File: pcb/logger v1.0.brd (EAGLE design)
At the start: 59.8 x 53.3 mm, 29 parts, among them J1 MICRO-SDCARD-CONNECTOR-330006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, K1 RESET, U1 DS1307ZN-1900100P1, U2 CJ1117-3.3-1310190P1, U3 74VHCT125PW, X1 32.768KHZ

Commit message: Mostly wired up
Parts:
- turned I2C to 90 degrees
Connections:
- new net AREF: JP2.1, U$4.AREF
- new net D2: JP4.3, U$4.D2
- new net D3: JP4.4, U$4.D3
- new net D4: JP4.5, U$4.D4
- new net D5: JP4.6, U$4.D5
- new net D6: JP4.7, U$4.D6
- new net D7: JP4.8, U$4.D7
- new net D8: JP2.8, U$4.D8
- new net D9: JP2.7, U$4.D9
- new net N$55: U$4.SCL
- new net N$87: U$4.SDA
- new net RX: JP4.1, U$4.RX
- new net TX: JP4.2, U$4.TX
- net +3V3: now also U$4.3.3V
- net +5V: now also U$4.5V
- net GND: now also U$4.GND@0, U$4.GND@1, U$4.GND@2
- net MISO: now also U$4.D12
- net MOSI: now also U$4.D11
- net RESET: now also U$4.RES
- net SCK: now also U$4.D13
- net SD_CS: now also U$4.D10
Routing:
- net SD_CS: track 113.8 -> 71.0 mm, vias 1 -> 4
- net +5V: track 107.6 -> 140.0 mm, vias 3 -> 0
- net SCK: track 78.5 -> 102.3 mm, vias 0 -> 1
- net +3V3: track 90.4 -> 70.7 mm, vias 2 -> 0
- net GND: track 27.7 -> 44.8 mm, vias 0 -> 4
- net MISO: track 64.9 -> 76.4 mm, vias 0 -> 1
- net N$20: track 39.4 -> 49.2 mm, vias 0 -> 1
- net MOSI: track 77.4 -> 71.9 mm
- net SD_DATAIN: track 10.9 -> 15.9 mm, vias 0 -> 2
- net AREF: track 0.00 -> 3.77 mm
- net TX: track 0.00 -> 3.77 mm
- net D9: track 0.00 -> 3.77 mm
- net D8: track 0.00 -> 3.77 mm
- net D7: track 0.00 -> 3.77 mm
- net D5: track 0.00 -> 3.77 mm
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- added copper zone on layer 16, net GND

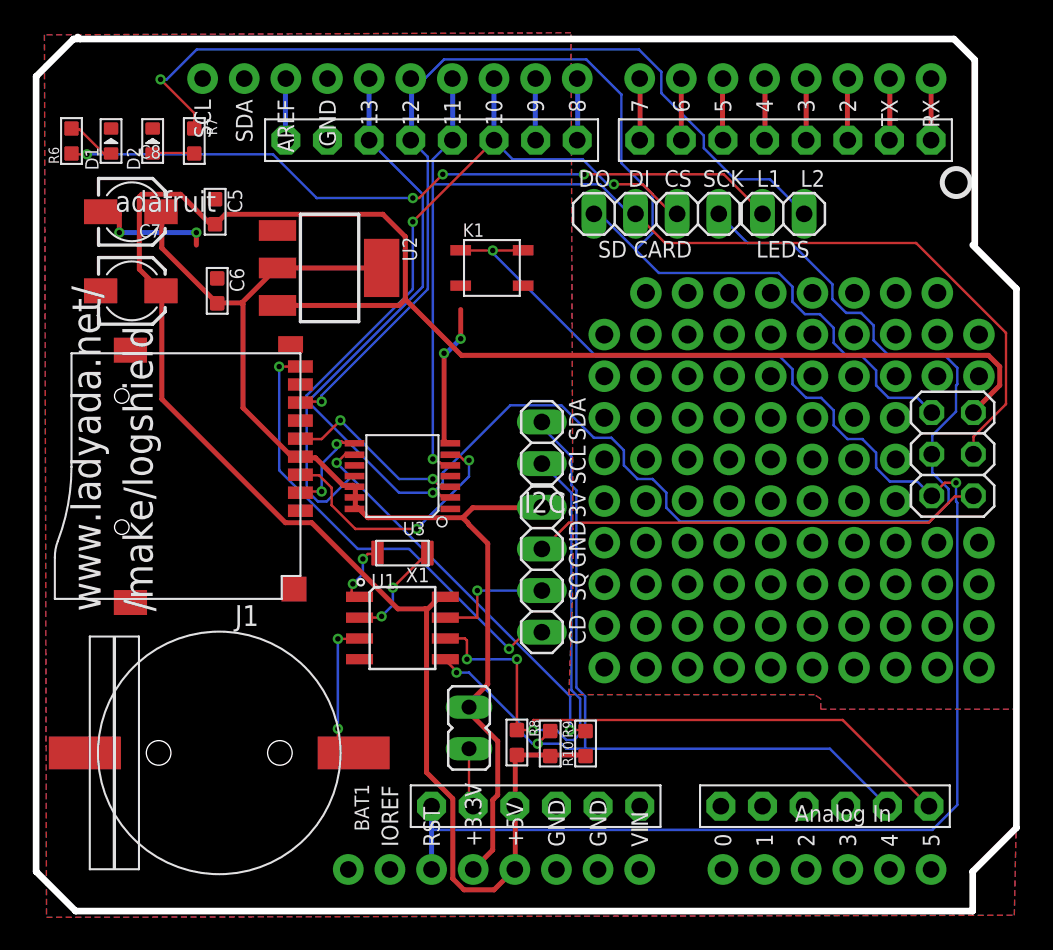
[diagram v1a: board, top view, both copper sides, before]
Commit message: Added extra LED's, finished wiring
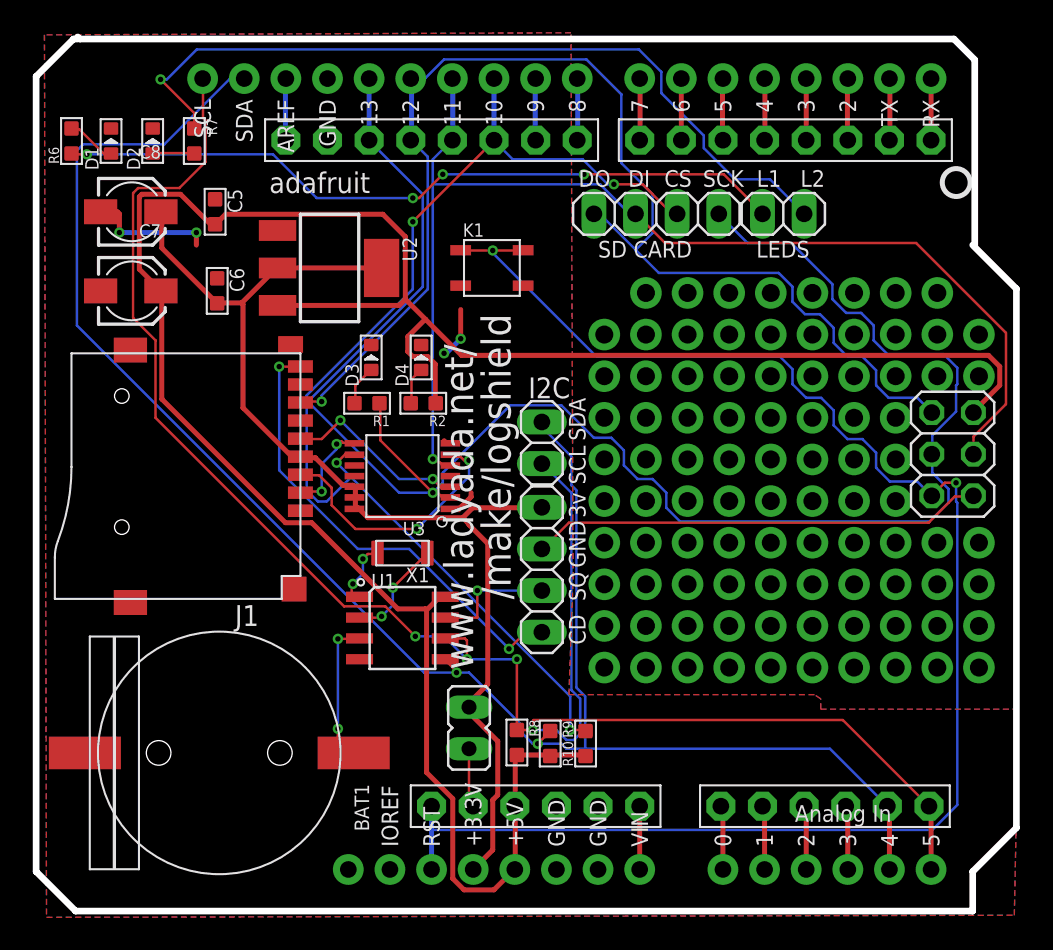
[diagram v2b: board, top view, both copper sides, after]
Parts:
- added D3: CLK, Discrete:LED-0603
- added D4: POWER, Discrete:LED-0603
- added R1, R2: 1k, Discrete:R0603
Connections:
- removed net N$55: U$4.SCL
- removed net N$87: U$4.SDA
- new net A0: JP9.1, U$4.A0
- new net A1: JP9.2, U$4.A1
- new net A2: JP9.3, U$4.A2
- new net A3: JP9.4, U$4.A3
- new net N$26: D3.+, R1.2
- new net N$40: D4.+, R2.2
- new net VIN: JP7.1, U$4.VIN
- net +5V: now also R2.1
- net GND: now also D3.-, D4.-
- net RTC_SCL: now also U$4.A5, U$4.SCL
- net RTC_SDA: now also U$4.A4, U$4.SDA
- net SCK: now also R1.1
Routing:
- net RTC_SDA: track 53.2 -> 111.8 mm
- net RTC_SCL: track 58.6 -> 112.3 mm, vias 3 -> 4
- net +5V: track 140.0 -> 146.8 mm
- net SCK: track 102.3 -> 109.1 mm
- net A1: track 0.00 -> 3.99 mm
- net A0: track 0.00 -> 3.99 mm
- net A3: track 0.00 -> 3.99 mm
- net A2: track 0.00 -> 3.99 mm
- net VIN: track 0.00 -> 3.86 mm
- net GND: track 44.8 -> 41.3 mm
- net N$26: track 0.00 -> 2.47 mm
- net N$40: track 0.00 -> 2.32 mm

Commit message: Changed and rerouted to match OPL availability
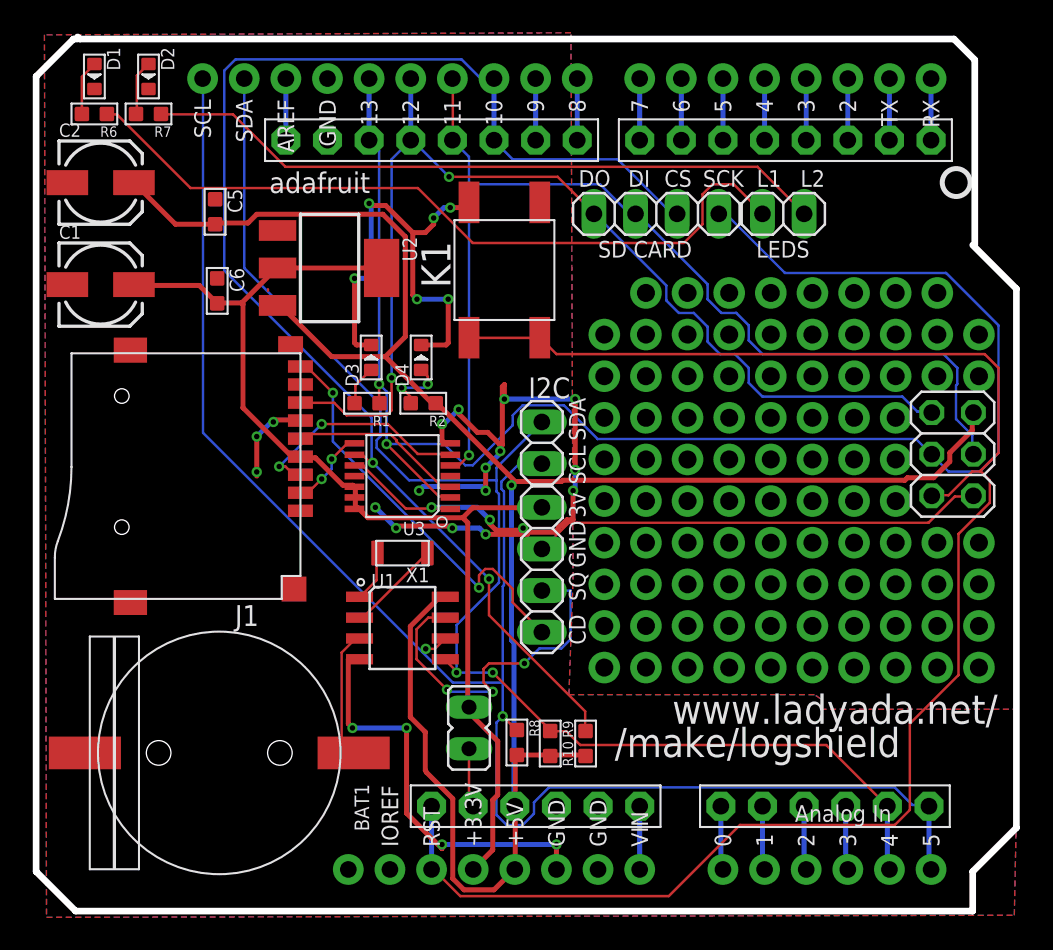
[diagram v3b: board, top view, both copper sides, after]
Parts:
- removed C7, C8: 100uF, Discrete:ELECTRO-SMD-A-3.8MM
- added C1, C2: 100uF, Discrete:ELECTRO-SMD-B-4.8MM
- K1: value RESET -> (none); device Discrete:4P-SMD-3.4X3.4X1.3H -> Discrete:4P-SMD-6.2X6.2X4H
- moved D1 4.07 mm to (13.0, 50.9), turned to 270 degrees
- moved D2 3.95 mm to (16.3, 50.9), turned to 270 degrees
- moved R7 3.25 mm to (16.3, 48.6), turned to 180 degrees
- moved R6 2.16 mm to (13.0, 48.6), turned to 180 degrees
- moved K1 0.77 mm to (38.0, 39.1), turned to 90 degrees
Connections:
- net +3V3: now also C1.+; no longer C8.+
- net +5V: now also C2.+; no longer C7.+
- net GND: now also C1.-, C2.-, K1.0B, K1.1B; no longer C7.-, C8.-, K1.B0, K1.B1
- net RESET: now also K1.0A, K1.1A; no longer K1.A0, K1.A1
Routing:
- net GND: track 41.3 -> 146.0 mm, vias 4 -> 30
- net RTC_SDA: track 111.8 -> 86.5 mm
- net +5V: track 146.8 -> 131.5 mm, vias 0 -> 1
- net SQW: track 7.54 -> 21.8 mm, vias 1 -> 3
- net SD_CS: track 71.0 -> 84.8 mm, vias 4 -> 2
- net SCK: track 109.1 -> 98.8 mm, vias 1 -> 2
- net MISO: track 76.4 -> 67.1 mm, vias 1 -> 2
- net N$20: track 49.2 -> 41.8 mm, vias 1 -> 0
- net RTC_SCL: track 112.3 -> 105.1 mm, vias 4 -> 2
- net MOSI: track 71.9 -> 66.1 mm
- net RESET: track 96.7 -> 102.3 mm, vias 2 -> 0
- net SD_CD: track 28.6 -> 25.1 mm
- net +3V3: track 70.7 -> 68.1 mm
- net SD_DATAIN: track 15.9 -> 13.8 mm
- net N$17: track 44.9 -> 46.6 mm, vias 4 -> 0
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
